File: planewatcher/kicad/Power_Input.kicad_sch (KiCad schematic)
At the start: 3 parts

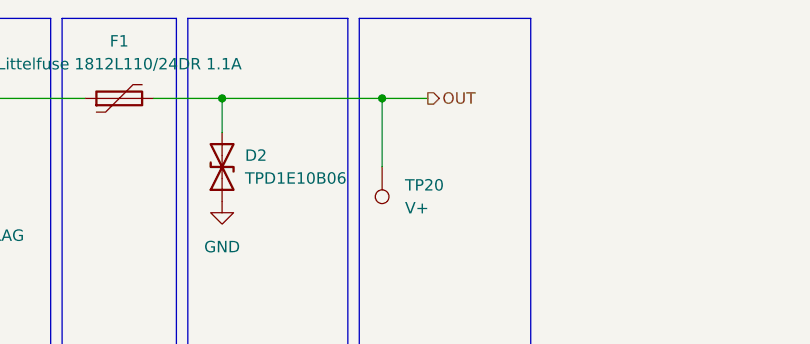
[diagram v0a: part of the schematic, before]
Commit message: Update PCB to include PPS output
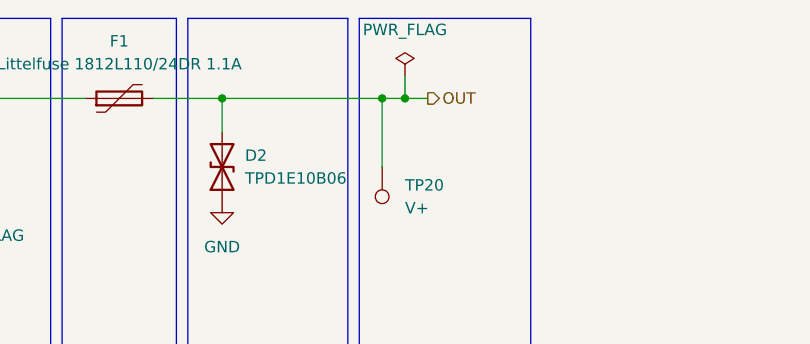
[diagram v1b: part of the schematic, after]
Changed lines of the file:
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@@
+	)
+	(junction
+		(at 132.08 88.9)
+		(diameter 0)
+		(color 0 0 0 0)
 	)
 	(junction
@@
 	(wire
 		(pts
-			(xy 85.09 88.9) (xy 96.52 88.9)
+			(xy 132.08 88.9) (xy 134.62 88.9)
 		)
 		(stroke
@@
 	(wire
 		(pts
-			(xy 111.76 88.9) (xy 111.76 92.71)
+			(xy 85.09 88.9) (xy 96.52 88.9)
 		)
 		(stroke
@@
 	(wire
 		(pts
-			(xy 129.54 88.9) (xy 134.62 88.9)
+			(xy 111.76 88.9) (xy 111.76 92.71)
 		)
 		(stroke
@@
 		)
 	)
+	(wire
+		(pts
+			(xy 129.54 88.9) (xy 132.08 88.9)
+		)
+		(stroke
+			(width 0)
+			(type default)
+		)
+	)
 	(polyline
 		(pts
@@
 		(pts
 			(xy 129.54 96.52) (xy 129.54 88.9)
+		)
+		(stroke
+			(width 0)
+			(type default)
+		)
+	)
+	(wire
+		(pts
+			(xy 132.08 86.36) (xy 132.08 88.9)
 		)
 		(stroke
@@
 					(unit 1)
 				)
+			)
+		)
+	)
+	(symbol
+		(lib_id "power:PWR_FLAG")
+		(at 132.08 86.36 0)
+		(unit 1)
+		(body_style 1)
+		(exclude_from_sim no)
+		(in_bom yes)
+		(on_board yes)
+		(in_pos_files yes)
+		(dnp no)
+		(fields_autoplaced yes)
+		(property "Reference" "#FLG01"
+			(at 132.08 84.455 0)
+			(hide yes)
+			(show_name no)
+			(do_not_autoplace no)
+			(effects
+				(font
+					(size 1.27 1.27)
+				)
+			)
+		)
+		(property "Value" "PWR_FLAG"
+			(at 132.08 81.28 0)
+			(show_name no)
+			(do_not_autoplace no)
+			(effects
+				(font
+					(size 1.27 1.27)
+				)
+			)
+		)
+		(property "Footprint" ""
+			(at 132.08 86.36 0)
+			(hide yes)
+			(show_name no)
+			(do_not_autoplace no)
+			(effects
+				(font
+					(size 1.27 1.27)
+				)
+			)
+		)
+		(property "Datasheet" ""
+			(at 132.08 86.36 0)
+			(hide yes)
+			(show_name no)
+			(do_not_autoplace no)
+			(effects
+				(font
+					(size 1.27 1.27)
+				)
+			)
+		)
+		(property "Description" "Special symbol for telling ERC where power comes from"
+			(at 132.08 86.36 0)
+			(hide yes)
+			(show_name no)
+			(do_not_autoplace no)
+			(effects
+				(font
+					(size 1.27 1.27)
+				)
+			)
+		)
+		(pin "1"
+		)
+		(instances
+			(project "planewatcher"
+				(path "/7a4a4324-e8b8-4d06-b75a-28095d4e9f10/5ac3603d-bbeb-44f4-b422-6252fe26d95e"
+					(reference "#FLG01")
+					(unit 1)
+				)

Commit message: Change all test point footprints to TestPoint_THTPad_D1.0mm_Drill0.5mm
Had to move TP15 slightly to prevent it shorting to 3V3.
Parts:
- TP20: footprint TestPoint:TestPoint_Pad_D1.0mm -> TestPoint:TestPoint_THTPad_D1.0mm_Drill0.5mm
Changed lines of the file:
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@@
 			)
 		)
-		(property "Footprint" "TestPoint:TestPoint_Pad_D1.0mm"
+		(property "Footprint" "TestPoint:TestPoint_THTPad_D1.0mm_Drill0.5mm"
 			(at 124.46 96.52 0)
 			(hide yes)
